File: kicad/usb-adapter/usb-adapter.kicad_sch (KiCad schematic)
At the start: 3 parts, among them J1 USB-A plug, port A, J2 USB-A plug, port B, J3 To main board

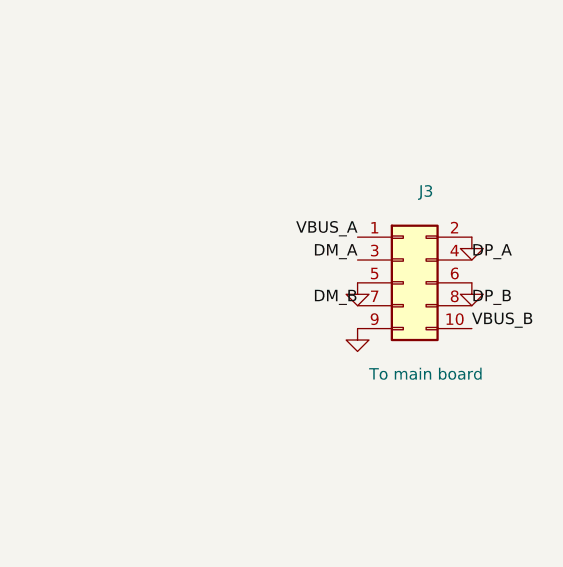
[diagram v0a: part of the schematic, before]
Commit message: Pi USB ribbons: 8-way - boxed 2 x 4 IDC on the main board, plain 2 x 4 header on the adapters
Pinout in ribbon order: VBUS A, GND, D- A, D+ A, GND, D- B, D+ B, VBUS B.
Symbol ids kept, so Update PCB swaps the footprints in place.

Co-Authored-By: Claude Opus 5.5 <noreply@anthropic.com>
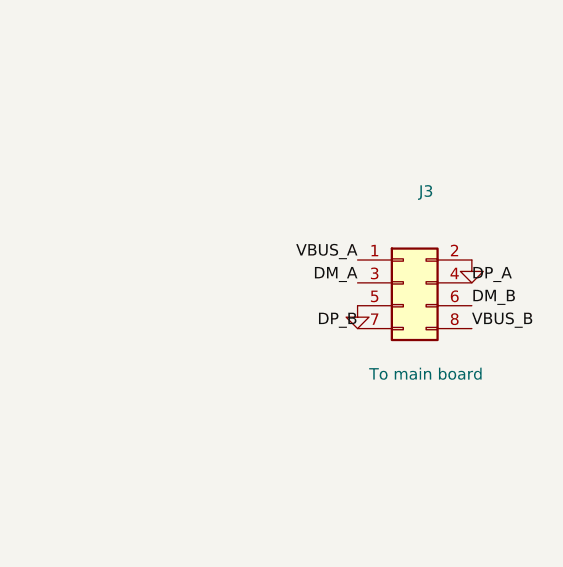
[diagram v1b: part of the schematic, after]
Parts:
- J3: footprint Connector_IDC:IDC-Header_2x05_P2.54mm_Vertical -> Connector_PinHeader_2.54mm:PinHeader_2x04_P2.54mm_Vertical; symbol Connector_Generic:Conn_02x05_Odd_Even -> Connector_Generic:Conn_02x04_Odd_Even
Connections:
- net DM_B: now also J3.6 (Pin_6); no longer J3.7 (Pin_7)
- net DP_B: now also J3.7 (Pin_7); no longer J3.8 (Pin_8)
- net GND: no longer J3.6 (Pin_6), J3.9 (Pin_9)
- net VBUS_B: now also J3.8 (Pin_8); no longer J3.10 (Pin_10)
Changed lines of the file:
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@@
 		(instances (project "usb-adapter" (path "/9158d672-1858-5b79-ba31-28ce8190e675" (reference "#PWR04") (unit 1))))
 	)
-	(symbol (lib_id "Connector_Generic:Conn_02x05_Odd_Even") (at 127 66.04 0) (unit 1) (exclude_from_sim no) (in_bom yes) (on_board yes) (dnp no)
+	(symbol (lib_id "Connector_Generic:Conn_02x04_Odd_Even") (at 127 66.04 0) (unit 1) (exclude_from_sim no) (in_bom yes) (on_board yes) (dnp no)
 		(property "Reference" "J3" (at 129.54 55.88 0) (effects (font (size 1.27 1.27))))
 		(property "Value" "To main board" (at 129.54 76.2 0) (effects (font (size 1.27 1.27))))
-		(property "Footprint" "Connector_IDC:IDC-Header_2x05_P2.54mm_Vertical" (at 127 66.04 0) (effects (font (size 1.27 1.27)) (hide yes)))
+		(property "Footprint" "Connector_PinHeader_2.54mm:PinHeader_2x04_P2.54mm_Vertical" (at 127 66.04 0) (effects (font (size 1.27 1.27)) (hide yes)))
 		(property "Datasheet" "" (at 127 66.04 0) (effects (font (size 1.27 1.27)) (hide yes)))
 		(pin "1")
@@
 		(pin "7")
 		(pin "8")
-		(pin "9")
-		(pin "10")
 		(instances (project "usb-adapter" (path "/9158d672-1858-5b79-ba31-28ce8190e675" (reference "J3") (unit 1))))
 	)
-	(label "VBUS_A" (at 121.92 60.96 180) (effects (font (size 1.27 1.27)) (justify right bottom)))
-	(symbol (lib_id "power:GND") (at 134.62 60.96 0) (unit 1) (exclude_from_sim no) (in_bom no) (on_board yes) (dnp no)
-		(property "Reference" "#PWR05" (at 137.16 50.8 0) (effects (font (size 1.27 1.27)) (hide yes)))
-		(property "Value" "GND" (at 137.16 71.12 0) (effects (font (size 1.27 1.27)) (hide yes)))
-		(property "Footprint" "" (at 134.62 60.96 0) (effects (font (size 1.27 1.27)) (hide yes)))
-		(property "Datasheet" "" (at 134.62 60.96 0) (effects (font (size 1.27 1.27)) (hide yes)))
+	(label "VBUS_A" (at 121.92 63.5 180) (effects (font (size 1.27 1.27)) (justify right bottom)))
+	(symbol (lib_id "power:GND") (at 134.62 63.5 0) (unit 1) (exclude_from_sim no) (in_bom no) (on_board yes) (dnp no)
+		(property "Reference" "#PWR05" (at 137.16 53.34 0) (effects (font (size 1.27 1.27)) (hide yes)))
+		(property "Value" "GND" (at 137.16 73.66 0) (effects (font (size 1.27 1.27)) (hide yes)))
+		(property "Footprint" "" (at 134.62 63.5 0) (effects (font (size 1.27 1.27)) (hide yes)))
+		(property "Datasheet" "" (at 134.62 63.5 0) (effects (font (size 1.27 1.27)) (hide yes)))
 		(pin "1")
 		(instances (project "usb-adapter" (path "/9158d672-1858-5b79-ba31-28ce8190e675" (reference "#PWR05") (unit 1))))
 	)
-	(label "DM_A" (at 121.92 63.5 180) (effects (font (size 1.27 1.27)) (justify right bottom)))
-	(label "DP_A" (at 134.62 63.5 0) (effects (font (size 1.27 1.27)) (justify left bottom)))
-	(symbol (lib_id "power:GND") (at 121.92 66.04 0) (unit 1) (exclude_from_sim no) (in_bom no) (on_board yes) (dnp no)
-		(property "Reference" "#PWR06" (at 124.46 55.88 0) (effects (font (size 1.27 1.27)) (hide yes)))
-		(property "Value" "GND" (at 124.46 76.2 0) (effects (font (size 1.27 1.27)) (hide yes)))
-		(property "Footprint" "" (at 121.92 66.04 0) (effects (font (size 1.27 1.27)) (hide yes)))
-		(property "Datasheet" "" (at 121.92 66.04 0) (effects (font (size 1.27 1.27)) (hide yes)))
+	(label "DM_A" (at 121.92 66.04 180) (effects (font (size 1.27 1.27)) (justify right bottom)))
+	(label "DP_A" (at 134.62 66.04 0) (effects (font (size 1.27 1.27)) (justify left bottom)))
+	(symbol (lib_id "power:GND") (at 121.92 68.58 0) (unit 1) (exclude_from_sim no) (in_bom no) (on_board yes) (dnp no)
+		(property "Reference" "#PWR06" (at 124.46 58.42 0) (effects (font (size 1.27 1.27)) (hide yes)))
+		(property "Value" "GND" (at 124.46 78.74 0) (effects (font (size 1.27 1.27)) (hide yes)))
+		(property "Footprint" "" (at 121.92 68.58 0) (effects (font (size 1.27 1.27)) (hide yes)))
+		(property "Datasheet" "" (at 121.92 68.58 0) (effects (font (size 1.27 1.27)) (hide yes)))
 		(pin "1")
 		(instances (project "usb-adapter" (path "/9158d672-1858-5b79-ba31-28ce8190e675" (reference "#PWR06") (unit 1))))
 	)
-	(symbol (lib_id "power:GND") (at 134.62 66.04 0) (unit 1) (exclude_from_sim no) (in_bom no) (on_board yes) (dnp no)
-		(property "Reference" "#PWR07" (at 137.16 55.88 0) (effects (font (size 1.27 1.27)) (hide yes)))
-		(property "Value" "GND" (at 137.16 76.2 0) (effects (font (size 1.27 1.27)) (hide yes)))
-		(property "Footprint" "" (at 134.62 66.04 0) (effects (font (size 1.27 1.27)) (hide yes)))
-		(property "Datasheet" "" (at 134.62 66.04 0) (effects (font (size 1.27 1.27)) (hide yes)))
-		(pin "1")
-		(instances (project "usb-adapter" (path "/9158d672-1858-5b79-ba31-28ce8190e675" (reference "#PWR07") (unit 1))))
-	)
-	(label "DM_B" (at 121.92 68.58 180) (effects (font (size 1.27 1.27)) (justify right bottom)))
-	(label "DP_B" (at 134.62 68.58 0) (effects (font (size 1.27 1.27)) (justify left bottom)))
-	(symbol (lib_id "power:GND") (at 121.92 71.12 0) (unit 1) (exclude_from_sim no) (in_bom no) (on_board yes) (dnp no)
-		(property "Reference" "#PWR08" (at 124.46 60.96 0) (effects (font (size 1.27 1.27)) (hide yes)))
-		(property "Value" "GND" (at 124.46 81.28 0) (effects (font (size 1.27 1.27)) (hide yes)))
-		(property "Footprint" "" (at 121.92 71.12 0) (effects (font (size 1.27 1.27)) (hide yes)))
-		(property "Datasheet" "" (at 121.92 71.12 0) (effects (font (size 1.27 1.27)) (hide yes)))
-		(pin "1")
-		(instances (project "usb-adapter" (path "/9158d672-1858-5b79-ba31-28ce8190e675" (reference "#PWR08") (unit 1))))
-	)
+	(label "DM_B" (at 134.62 68.58 0) (effects (font (size 1.27 1.27)) (justify left bottom)))
+	(label "DP_B" (at 121.92 71.12 180) (effects (font (size 1.27 1.27)) (justify right bottom)))
 	(label "VBUS_B" (at 134.62 71.12 0) (effects (font (size 1.27 1.27)) (justify left bottom)))
 	(symbol (lib_id "power:GND") (at 25.4 25.4 0) (unit 1) (exclude_from_sim no) (in_bom no) (on_board yes) (dnp no)
